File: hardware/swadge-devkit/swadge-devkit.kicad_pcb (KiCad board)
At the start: 2 copper layers, 63.7 x 89.4 mm, 69 parts, among them J1 USB_B_Micro, SW1 SW_SPDT, SW2 4-1437565-2, SW3 4-1437565-2, SW4 4-1437565-2, SW5 4-1437565-2, U1 GS321-TR, U2 AP1117-33, U3 SAO, U4 ESP-13-WROOM-02D, U5 BUS_PCIexpress, U6 DISP_OLED_UG-2864HSWEG01, U7 MMA8452Q, U8 MSA300, U9 QMA6981

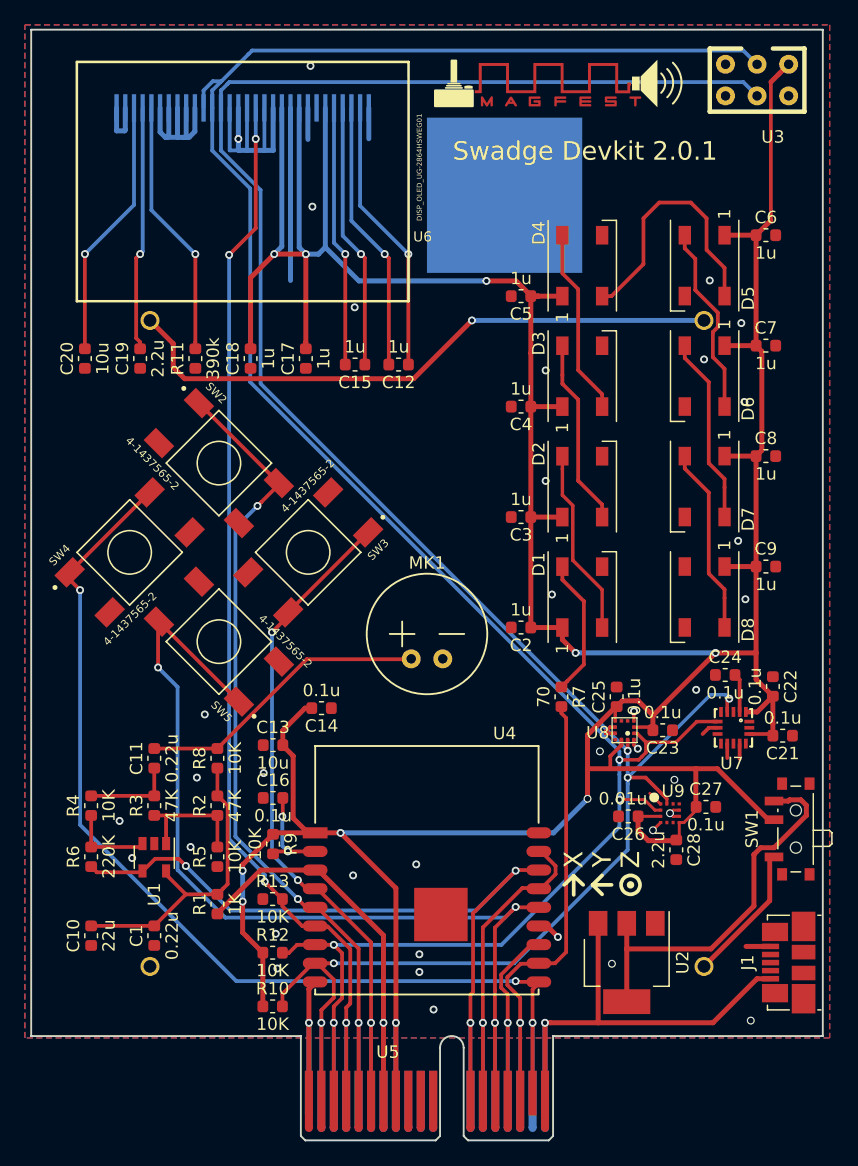
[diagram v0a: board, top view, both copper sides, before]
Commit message: Fixed 3d model paths for all projects
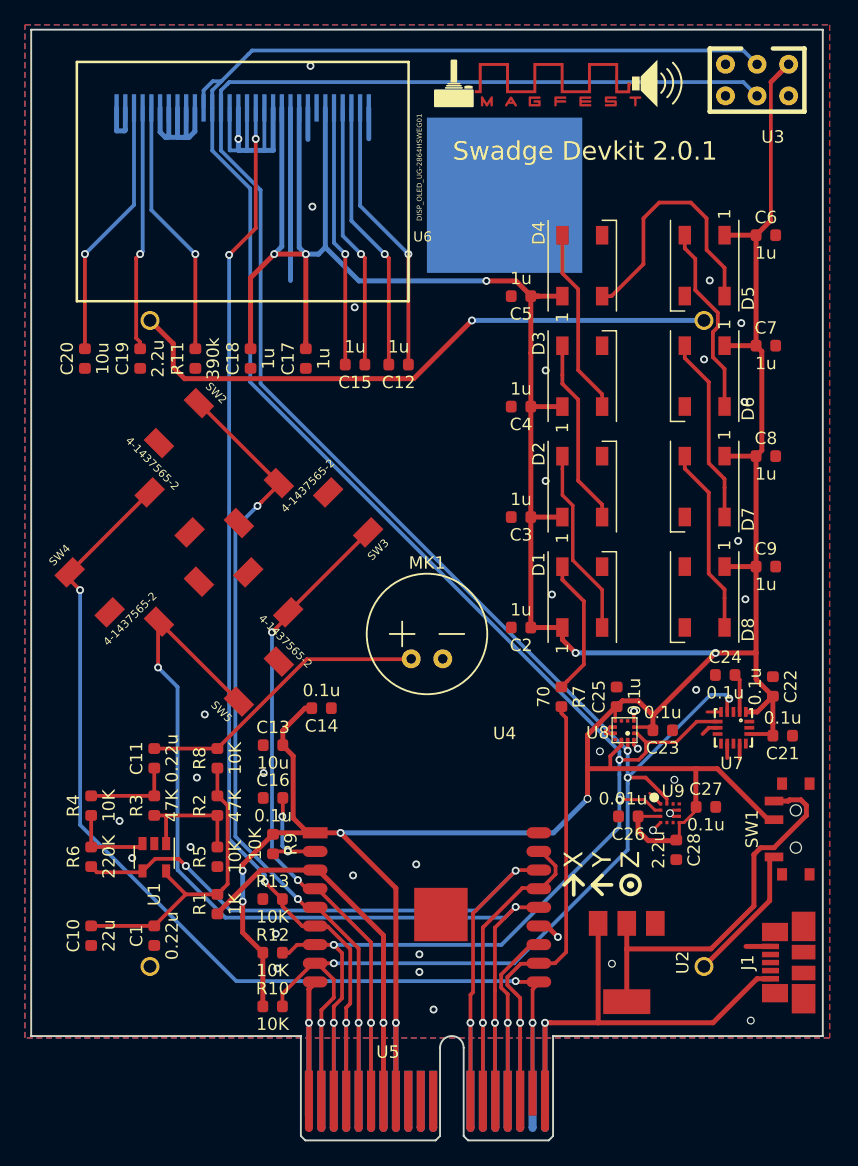
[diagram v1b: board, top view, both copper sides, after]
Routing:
- net GND: track 88.4 -> 89.5 mm
